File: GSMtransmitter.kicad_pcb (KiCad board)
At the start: 2 copper layers, 69 x 83 mm, 120 parts, among them J1 Conn_01x06_Pin, J10 HJ-SMA405, J2 Conn_02x02_2.54, J3 Conn_01x05, J4 8P8C_DS1134, J5 Conn_DEGSON_01x02_Pin, J6 Conn_DEGSON_01x02_Pin, J7 Conn_DEGSON_01x02_Pin, J8 Conn_DEGSON_01x02_Pin, J9 1042240820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

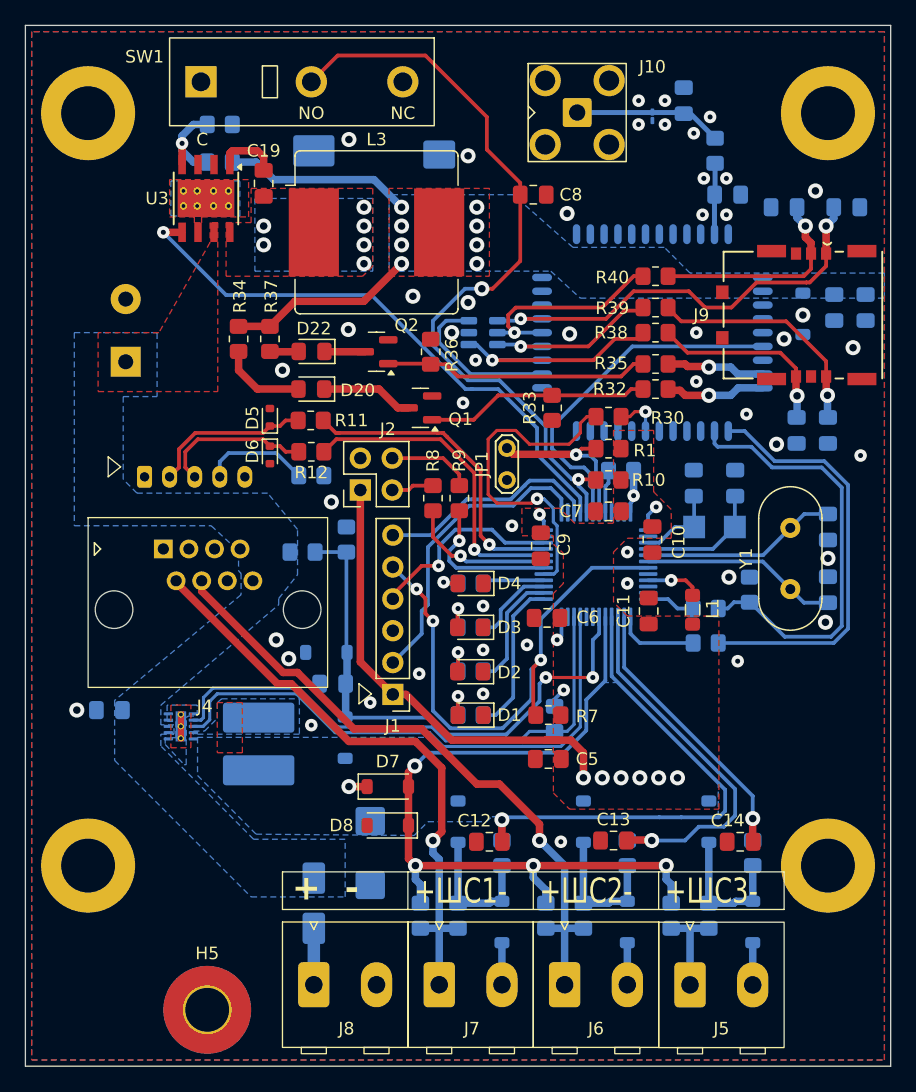
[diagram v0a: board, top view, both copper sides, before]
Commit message: Minor changes in PCB for manufacturing
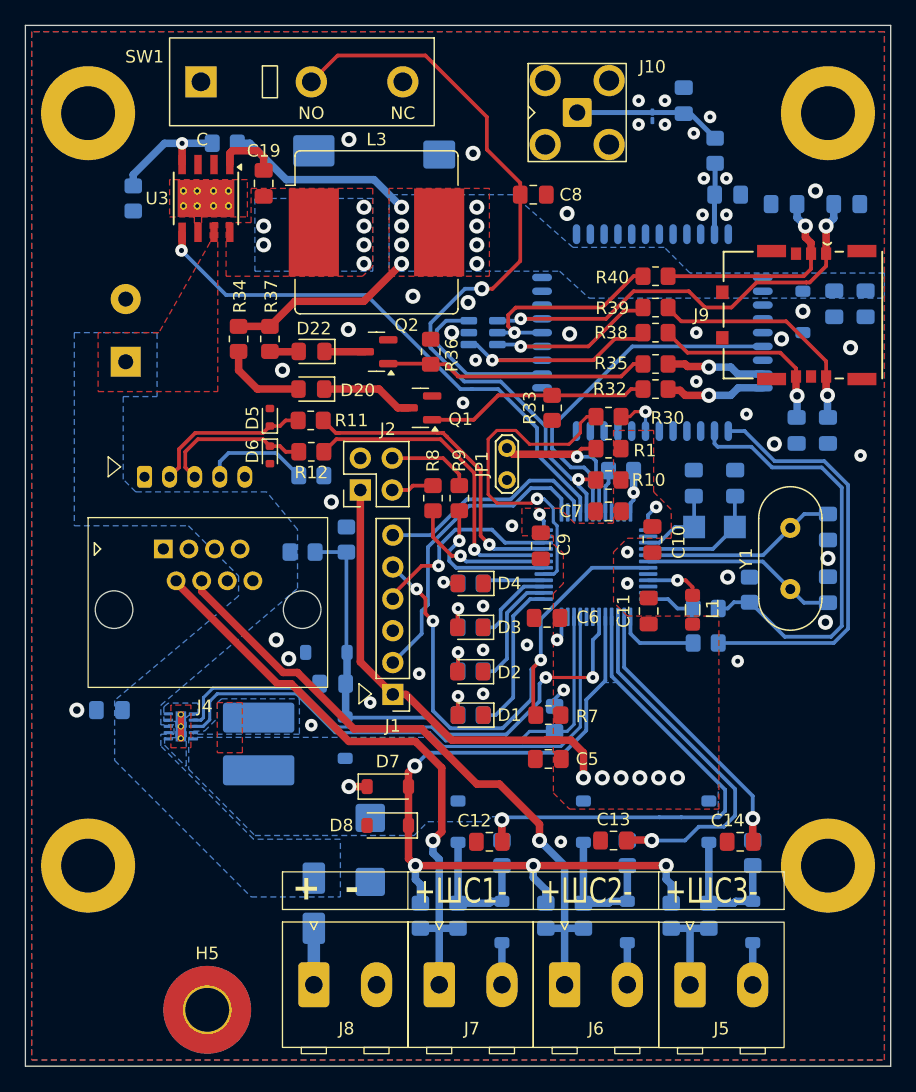
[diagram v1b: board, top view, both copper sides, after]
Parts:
- moved R26 9.08 mm to (36.6, 36.8), turned to 90 degrees
- moved R27 1.55 mm to (43.9, 32.4)
- moved C21 0.30 mm to (92.5, 45.2)
- moved C22 0.30 mm to (95.0, 45.2)
- moved C18 0.25 mm to (55.5, 88.8)
- moved C23 0.25 mm to (93.5, 37.2)
- moved C24 0.25 mm to (88.5, 37.2)
- moved D19 0.15 mm to (90.0, 45.9)
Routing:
- net Net-(U3-VSENSE): track 7.64 -> 9.93 mm
- net /4V_ENABLE: track 45.9 -> 43.8 mm
